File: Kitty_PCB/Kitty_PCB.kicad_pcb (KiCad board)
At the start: 2 copper layers, 90.8 x 89.8 mm, 1 part, among them U1 PicoW

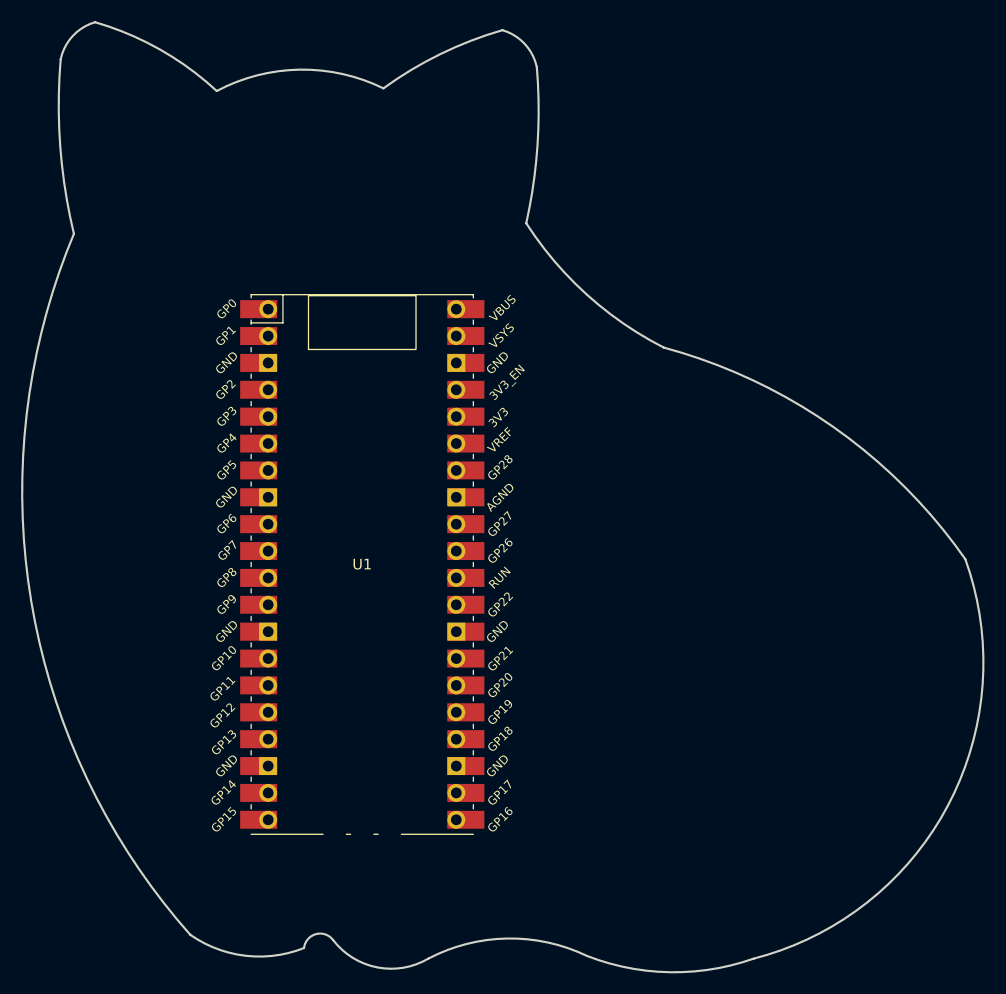
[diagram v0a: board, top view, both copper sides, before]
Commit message: Added some extra ground pins
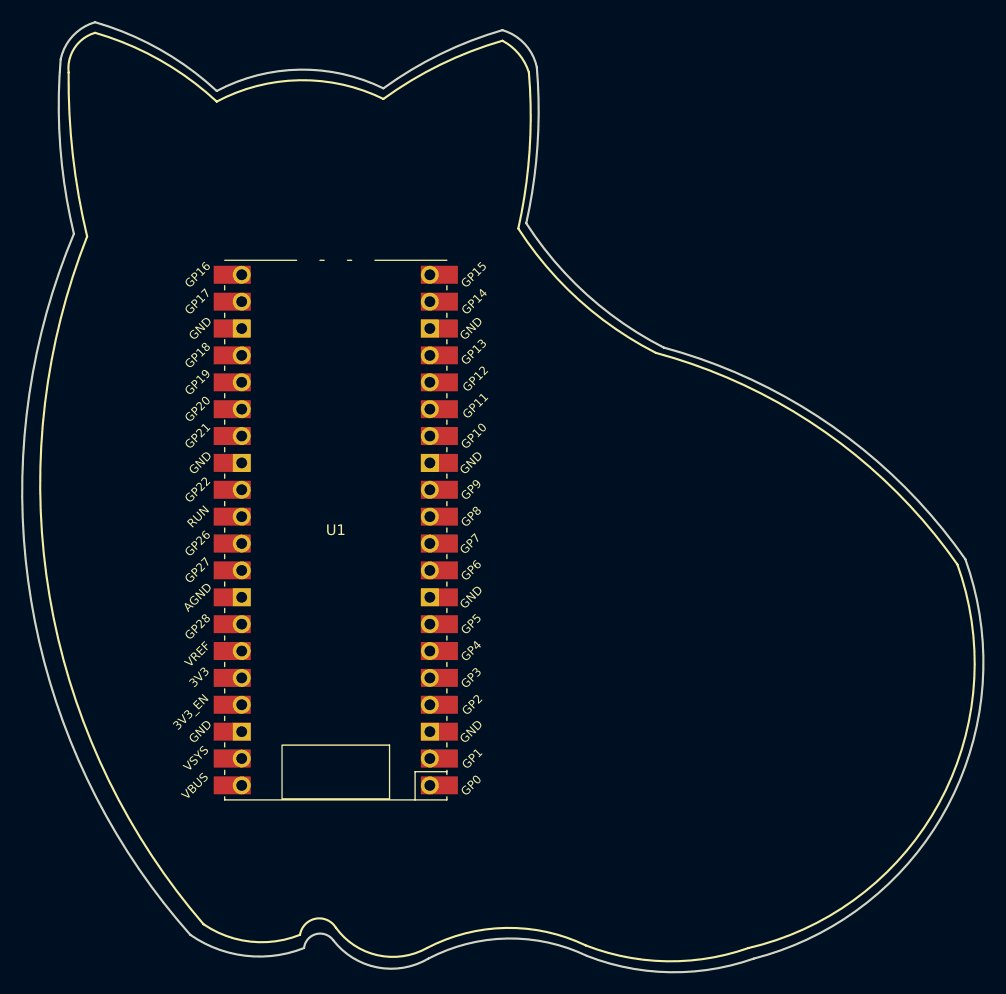
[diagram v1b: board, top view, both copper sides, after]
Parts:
- moved U1 4.10 mm to (215.8, 104.8), turned to 180 degrees

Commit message: Edits
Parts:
- removed U1: PicoW, RPi_Pico:RPi_PicoW_SMD_TH
- added J3: Conn_01x06, Connector_PinHeader_2.54mm:PinHeader_1x06_P2.54mm_Vertical, F.Cu at (212.4, 75.2)
- added REF**: SW_Cherry_MX_1.00u_PCB, Button_Switch_Keyboard:SW_Cherry_MX_1.00u_PCB, F.Cu at (214.8, 105.0)
- added REF**: SW_Cherry_MX_1.00u_PCB, Button_Switch_Keyboard:SW_Cherry_MX_1.00u_PCB, F.Cu at (244.5, 105.0)
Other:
- board size 90.8 x 89.8 mm -> 90.8 x 99.8 mm

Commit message: push
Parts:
- removed J3: Conn_01x06, Connector_PinHeader_2.54mm:PinHeader_1x06_P2.54mm_Vertical
- removed REF** (x2): SW_Cherry_MX_1.00u_PCB, Button_Switch_Keyboard:SW_Cherry_MX_1.00u_PCB
- added H1: MountingHole_Pad, MountingHole:MountingHole_3mm_Pad_Via, F.Cu at (111.2, 56.2)
- added H2: MountingHole_Pad, MountingHole:MountingHole_3mm_Pad_Via, F.Cu at (146.2, 57.2)
- added H3: MountingHole_Pad, MountingHole:MountingHole_3mm_Pad_Via, F.Cu at (186.8, 104.5)
- added H4: MountingHole_Pad, MountingHole:MountingHole_3mm_Pad_Via, F.Cu at (164.0, 133.2)
- added H5: MountingHole_Pad, MountingHole:MountingHole_3mm_Pad_Via, F.Cu at (124.5, 132.0)
- added H6: MountingHole_Pad, MountingHole:MountingHole_3mm_Pad_Via, F.Cu at (144.4, 100.9)
- added J1: Conn_01x04, Connector_PinSocket_2.54mm:PinSocket_1x04_P2.54mm_Vertical, F.Cu at (125.3, 59.7)
- added SW1: SW_Push, Button_Switch_Keyboard:SW_Cherry_MX_1.00u_PCB, F.Cu at (132.4, 95.9)
- added SW2: SW_Push, Button_Switch_Keyboard:SW_Cherry_MX_1.00u_PCB, F.Cu at (163.0, 96.0)
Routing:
- net Net-(J1-Pad4): track 0.00 -> 55.1 mm
- net Net-(J1-Pad3): track 0.00 -> 52.4 mm
- net Net-(J1-Pad2): track 0.00 -> 39.8 mm
- net Net-(J1-Pad1): track 0.00 -> 39.0 mm
- added copper zone on B.Cu, net GND
- added copper zone on F.Cu, net GND
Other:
- board size 90.8 x 99.8 mm -> 90.8 x 89.8 mm
